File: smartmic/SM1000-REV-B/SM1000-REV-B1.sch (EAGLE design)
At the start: 173 parts, among them CN1 HDR100-3, CN10 MJ-3523-SMT, CN11 HDR100-3, CN12 DF11-16DS, CN2 MOLEX-MINI-B-SMT, CN3 RASM712PX, CN4 RJ-45, CN5 MJ-3523-SMT, CN6 MJ-3523-SMT, CN7 MJ-3523-SMT, CN8 MJ-3523-SMT, CN9 MJ-3523-SMT, J1 JMP-2PIN, J2 JMP-2PIN, J3 JMP-2PIN, J4 JMP-2PIN, J5 JMP-2PIN, J7 JMP-2PIN, P1 TPAD50, P10 TPAD50, P11 TPAD50, P12 TPAD50, P13 TPAD50, P14 TPAD50, P15 TPAD50, P16 TPAD50, P17 TPAD50, P18 TPAD50, P19 TPAD50, P2 TPAD50, P20 TPAD50, P3 TPAD50, P4 TPAD50, P5 TPAD50, P6 TPAD50, P7 TPAD50, P8 TPAD50, P9 TPAD50, SW1 SW-BOURNS-7914S, SW2 SW-BOURNS-7914S, SW3 DPDT, SW4 SW-BOURNS-7914S, T1 SM-LP-5001, T2 SM-LP-5001, U1 STM32F405, U2 LD3985M33R, U3 STMPS2141, U4 EMIF02-USB03F2, U5 TPS54329E, U6 LMV341, U7 LMV341, U8 LM386M-1, U9 LMV341

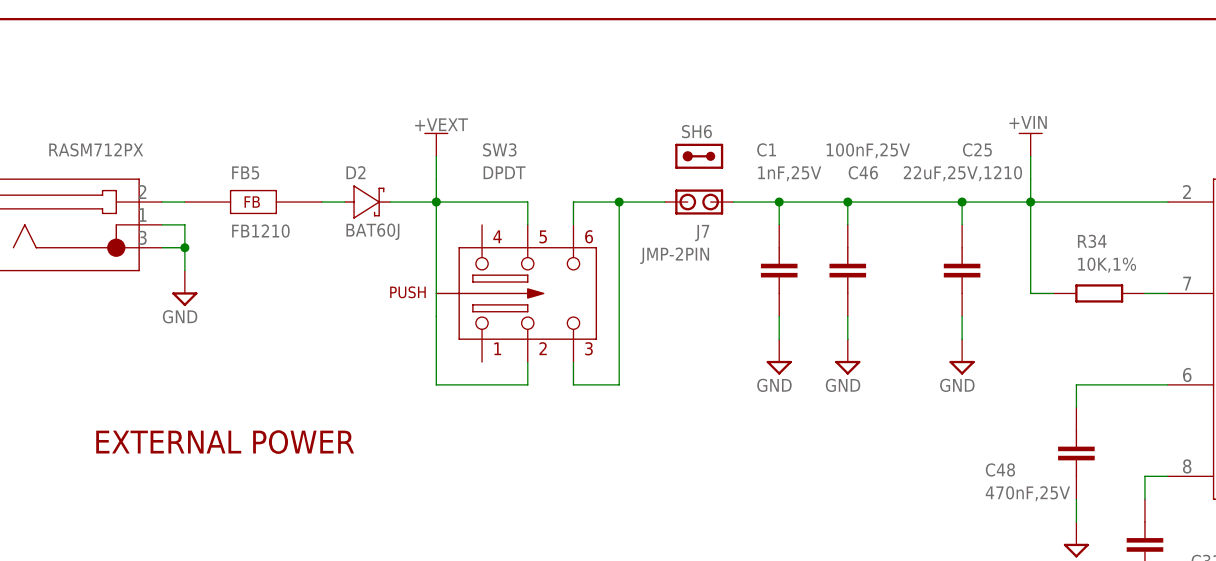
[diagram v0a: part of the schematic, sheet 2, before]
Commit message: 
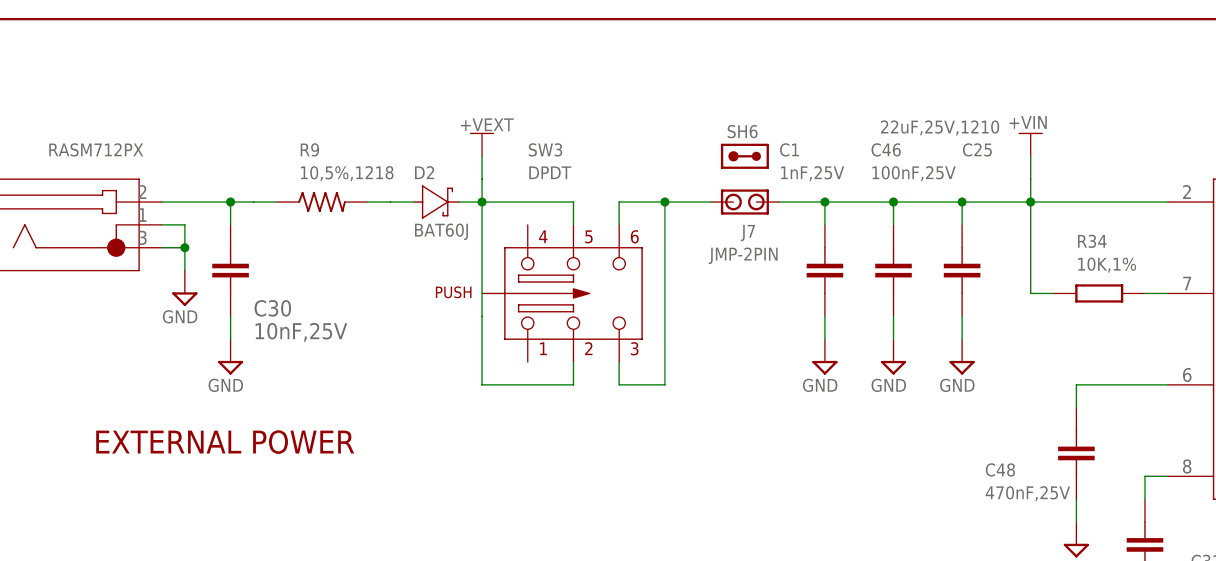
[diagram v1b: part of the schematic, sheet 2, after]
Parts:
- removed FB5: FB1210, _RoweTel:FB1210
- added C30: 10nF,25V, AA-ipc-7351-capacitor:CAPACITOR_0603
- added R9: 10,5%,1218, SM1000:RCL1218
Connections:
- net GND: now also C30.2
- net N$24: now also R9.2; no longer FB5.2
- net N$77: now also C30.1, R9.1; no longer FB5.1
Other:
- moved on the sheet: C1, C46, D2, J7, SH6, SW3

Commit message: The latest SM1000-REV-B1 PCB design - RGB
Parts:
- added R11: 100,1%, AA-ipc-7351-resistor:RESISTOR_0603
- C34: value 100pF,50V -> 1nF,50V
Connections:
- net N$11 renamed PE0
- net N$13 renamed PE1
- net N$14 renamed PE2
- net N$15 renamed PE3
- removed net !BACK!: R8.1, SW4.P$3, SW4.P$4, U1A.PD1
- removed net !SELECT!: R7.1, SW2.P$3, SW2.P$4, U1A.PD0
- new net BACK: R8.2, SW4.P$1, SW4.P$2, U1A.PD1
- new net N$26: FB4.2, R11.1
- new net SELECT: R7.2, SW2.P$1, SW2.P$2, U1A.PD0
- net GND: now also R7.1, R8.1; no longer SW2.P$1, SW2.P$2, SW4.P$1, SW4.P$2
- net N$25: now also R11.2; no longer FB4.2
- net VDD: now also SW2.P$3, SW2.P$4, SW4.P$3, SW4.P$4; no longer R7.2, R8.2
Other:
- note added: "06/17/2014"
- note added: "44. Add test point P20 (+VIN )."
- note added: "45. Added 1nf cap in parallel with C46."
- note added: "46. Ad 10nF cap across CN3."
- note added: "47. Replaced FB5 with 10 Ohm 1206 Wide resistor."
- note added: "48. Aded 1K resistor in series with FB4."
- note added: "49. Changed C34 to 1nF."
- note added: "50. Changed Select & Back circuits to match PTT."
- note added: "Complete"
- note removed: "40. Add test point P20 (+VIN )."
- note removed: "Change Log for SM1000 PCB"
- note removed: "XX. Test."
